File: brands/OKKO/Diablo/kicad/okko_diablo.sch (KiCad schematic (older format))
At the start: 65 parts, among them P1 1M Log, P2 1M Lin, P3 1M Log, P4 100k Log, P5 100k Lin, P6 100k Lin, Q1 J201, Q2 J201, Q3 J201, Q4 J201, Q5 J201, Q6 J201, Q7 J201, T1 100k, T2 10k Log, T3 100k Log, T4 100k Log, T5 100k Lin

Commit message: OKKO Diablo schematic
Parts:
- P3: value 1M Log -> 500k Log
- P6: value 100k Lin -> 100k Log
- T1: value 100k -> 100k Lin
- T2: value 10k Log -> 5k Log
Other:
- note added: "Bass"
- note added: "Bass+"
- note added: "Body"
- note added: "Feed"
- note added: "Gain"
- note added: "Gain+"
- note added: "Level"
- note added: "Level+"
- note added: "Presence"
- note added: "Presence+"
- note added: "Tone"
- moved on the sheet: C15, C18, P6, Q7, R20, R21
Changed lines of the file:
@@
 P 3750 3250
 F 0 "T2" V 3650 3350 59  0000 C CNN
-F 1 "10k Log" H 3750 3100 59  0000 C CNN
+F 1 "5k Log" H 3750 3100 59  0000 C CNN
 F 2 "" H 3750 3250 60  0000 C CNN
 F 3 "" H 3750 3250 60  0000 C CNN
@@
 P 3050 2250
 F 0 "T1" H 2950 2350 59  0000 C CNN
-F 1 "100k" H 3050 2150 59  0000 C CNN
+F 1 "100k Lin" H 3050 2150 59  0000 C CNN
 F 2 "" H 3050 2250 60  0000 C CNN
 F 3 "" H 3050 2250 60  0000 C CNN
@@
 P 4800 5550
 F 0 "P3" V 4900 5700 59  0000 C CNN
-F 1 "1M Log" H 4800 5400 59  0000 C CNN
+F 1 "500k Log" H 4800 5400 59  0000 C CNN
 F 2 "" H 4800 5550 60  0000 C CNN
 F 3 "" H 4800 5550 60  0000 C CNN
@@
 L CAPACITOR C15
 U 1 1 54CC49C0
-P 6650 5350
-F 0 "C15" H 6650 5480 59  0000 C CNN
-F 1 "3.3n" H 6650 5210 59  0000 C CNN
-F 2 "" H 6650 5350 60  0000 C CNN
-F 3 "" H 6650 5350 60  0000 C CNN
-	1    6650 5350
+P 6650 5200
+F 0 "C15" H 6650 5330 59  0000 C CNN
+F 1 "3.3n" H 6650 5060 59  0000 C CNN
+F 2 "" H 6650 5200 60  0000 C CNN
+F 3 "" H 6650 5200 60  0000 C CNN
+	1    6650 5200
 	0    -1   1    0
 $EndComp
@@
 	6450 4700 6650 4700
 Wire Wire Line
-	6650 4450 6650 5200
+	6650 4450 6650 5050
 $Comp
 L POTENTIOMETER P5
@@
 Connection ~ 7450 4950
 Wire Wire Line
-	6900 4950 6650 4950
+	6650 4950 6900 4950
 $Comp
 L RESISTOR R20
 U 1 1 54CC9ED9
-P 7800 5050
-F 0 "R20" H 7800 5150 59  0000 C CNN
-F 1 "1M" H 7800 4950 59  0000 C CNN
-F 2 "" H 7650 5090 60  0000 C CNN
-F 3 "" H 7650 5090 60  0000 C CNN
-	1    7800 5050
+P 7950 5200
+F 0 "R20" H 7950 5300 59  0000 C CNN
+F 1 "1M" H 7950 5100 59  0000 C CNN
+F 2 "" H 7800 5240 60  0000 C CNN
+F 3 "" H 7800 5240 60  0000 C CNN
+	1    7950 5200
 	0    -1   -1   0
 $EndComp
@@
 L NJFET Q7
 U 1 1 54CC9F62
-P 8300 4700
-F 0 "Q7" H 8140 4590 59  0000 R CNN
-F 1 "J201" H 8140 4910 59  0000 R CNN
-F 2 "TO92" H 8030 4820 29  0001 C CNN
-F 3 "" H 8175 4750 60  0000 C CNN
-	1    8300 4700
+P 8450 4700
+F 0 "Q7" H 8290 4590 59  0000 R CNN
+F 1 "J201" H 8290 4910 59  0000 R CNN
+F 2 "TO92" H 8180 4820 29  0001 C CNN
+F 3 "" H 8325 4750 60  0000 C CNN
+	1    8450 4700
 	1    0    0    -1
 $EndComp
@@
 L GND #PWR024
 U 1 1 54CC9FF4
-P 7800 5250
-F 0 "#PWR024" H 7800 5350 30  0001 C CNN
-F 1 "GND" H 7800 5100 30  0001 C CNN
-F 2 "" H 7800 5250 60  0000 C CNN
-F 3 "" H 7800 5250 60  0000 C CNN
-	1    7800 5250
+P 7950 5400
+F 0 "#PWR024" H 7950 5500 30  0001 C CNN
+F 1 "GND" H 7950 5250 30  0001 C CNN
+F 2 "" H 7950 5400 60  0000 C CNN
+F 3 "" H 7950 5400 60  0000 C CNN
+	1    7950 5400
 	1    0    0    -1
 $EndComp
@@
 L V+ #PWR025
 U 1 1 54CCA035
-P 8300 4400
-F 0 "#PWR025" H 8300 4370 20  0001 C CNN
-F 1 "V+" H 8300 4530 59  0000 C CNN
-F 2 "" H 8300 4400 60  0000 C CNN
-F 3 "" H 8300 4400 60  0000 C CNN
-	1    8300 4400
-	1    0    0    -1
-$EndComp
-Wire Wire Line
-	7600 4700 8000 4700
-Wire Wire Line
-	7800 4850 7800 4700
-Connection ~ 7800 4700
+P 8450 4400
+F 0 "#PWR025" H 8450 4370 20  0001 C CNN
+F 1 "V+" H 8450 4530 59  0000 C CNN
+F 2 "" H 8450 4400 60  0000 C CNN
+F 3 "" H 8450 4400 60  0000 C CNN
+	1    8450 4400
+	1    0    0    -1
+$EndComp
+Wire Wire Line
+	7600 4700 8150 4700
+Wire Wire Line
+	7950 4700 7950 5000
+Connection ~ 7950 4700
 $Comp
 L RESISTOR R21
 U 1 1 54CCA8A4
-P 8300 5200
-F 0 "R21" H 8300 5300 59  0000 C CNN
-F 1 "4.7k" H 8300 5100 59  0000 C CNN
-F 2 "" H 8150 5240 60  0000 C CNN
-F 3 "" H 8150 5240 60  0000 C CNN
-	1    8300 5200
+P 8450 5200
+F 0 "R21" H 8450 5300 59  0000 C CNN
+F 1 "4.7k" H 8450 5100 59  0000 C CNN
+F 2 "" H 8300 5240 60  0000 C CNN
+F 3 "" H 8300 5240 60  0000 C CNN
+	1    8450 5200
 	0    -1   1    0
 $EndComp
@@
 L GND #PWR026
 U 1 1 54CCA9B3
-P 8300 5400
-F 0 "#PWR026" H 8300 5500 30  0001 C CNN
-F 1 "GND" H 8300 5250 30  0001 C CNN
-F 2 "" H 8300 5400 60  0000 C CNN
-F 3 "" H 8300 5400 60  0000 C CNN
-	1    8300 5400
+P 8450 5400
+F 0 "#PWR026" H 8450 5500 30  0001 C CNN
+F 1 "GND" H 8450 5250 30  0001 C CNN
+F 2 "" H 8450 5400 60  0000 C CNN
+F 3 "" H 8450 5400 60  0000 C CNN
+	1    8450 5400
 	1    0    0    -1
 $EndComp
@@
 L CAPACITOR C18
 U 1 1 54CCAB4B
-P 8650 4950
-F 0 "C18" H 8650 5080 59  0000 C CNN
-F 1 "100n" H 8650 4810 59  0000 C CNN
-F 2 "" H 8650 4950 60  0000 C CNN
-F 3 "" H 8650 4950 60  0000 C CNN
-	1    8650 4950
+P 8800 4950
+F 0 "C18" H 8800 5080 59  0000 C CNN
+F 1 "100n" H 8800 4810 59  0000 C CNN
+F 2 "" H 8800 4950 60  0000 C CNN
+F 3 "" H 8800 4950 60  0000 C CNN
+	1    8800 4950
 	-1   0    0    -1
 $EndComp
 Wire Wire Line
-	8300 4900 8300 5000
-Wire Wire Line
-	8300 4950 8500 4950
-Connection ~ 8300 4950
+	8450 4900 8450 5000
+Wire Wire Line
+	8450 4950 8650 4950
+Connection ~ 8450 4950
 $Comp
 L POTENTIOMETER P6
 U 1 1 54CCB094
-P 9050 5200
-F 0 "P6" V 9150 5350 59  0000 C CNN
-F 1 "100k Lin" H 9050 5050 59  0000 C CNN
-F 2 "" H 9050 5200 60  0000 C CNN
-F 3 "" H 9050 5200 60  0000 C CNN
-	1    9050 5200
+P 9200 5200
+F 0 "P6" V 9300 5350 59  0000 C CNN
+F 1 "100k Log" H 9200 5050 59  0000 C CNN
+F 2 "" H 9200 5200 60  0000 C CNN
+F 3 "" H 9200 5200 60  0000 C CNN
+	1    9200 5200
 	0    1    1    0
 $EndComp
 Wire Wire Line
-	9050 5000 9050 4950
-Wire Wire Line
-	9050 4950 8800 4950
+	9200 5000 9200 4950
+Wire Wire Line
+	9200 4950 8950 4950
 $Comp
 L GND #PWR027
 U 1 1 54CCB670
-P 9050 5400
-F 0 "#PWR027" H 9050 5500 30  0001 C CNN
-F 1 "GND" H 9050 5250 30  0001 C CNN
-F 2 "" H 9050 5400 60  0000 C CNN
-F 3 "" H 9050 5400 60  0000 C CNN
-	1    9050 5400
+P 9200 5400
+F 0 "#PWR027" H 9200 5500 30  0001 C CNN
+F 1 "GND" H 9200 5250 30  0001 C CNN
+F 2 "" H 9200 5400 60  0000 C CNN
+F 3 "" H 9200 5400 60  0000 C CNN
+	1    9200 5400
 	1    0    0    -1
 $EndComp
@@
 	4600 2700 4500 2700
 Wire Wire Line
-	6650 5500 6850 5500
-Wire Wire Line
-	6850 5500 6850 5800
+	6850 5450 6850 5800
 Wire Wire Line
 	6850 5800 6750 5800
-Text Label 2250 2850 2    60   ~ 0
+Text Label 2250 2850 2    60   ~ 12
 BoostIn
-Text Label 5250 2300 0    60   ~ 0
+Text Label 5250 2300 0    60   ~ 12
 BoostOut
 Wire Wire Line
 	5250 2300 5050 2300
-Text Label 1550 5250 2    60   ~ 0
+Text Label 1550 5250 2    60   ~ 12
 MainIn
 Connection ~ 1750 5250
-Text Label 9400 5200 0    60   ~ 0
+Text Label 9550 5200 0    60   ~ 12
 MainOut
 Wire Wire Line
-	9400 5200 9200 5200
+	9550 5200 9350 5200
+Wire Wire Line
+	6650 5500 6650 5350
+Wire Wire Line
+	6650 5450 6850 5450
+Connection ~ 6650 5450
+Connection ~ 7450 5900
+Connection ~ 3750 3050
+Connection ~ 4400 2400
+Text Notes 1250 5600 0    79   ~ 16
+Feed
+Text Notes 4400 4850 0    79   ~ 16
+Body
+Text Notes 4300 5600 0    79   ~ 16
+Gain
+Text Notes 7600 4550 0    79   ~ 16
+Tone
+Text Notes 8650 5350 0    79   ~ 16
+Level
+Text Notes 4900 1900 0    79   ~ 16
+Level+
+Text Notes 2500 2350 0    59   ~ 12
+Bass+
+Text Notes 4000 3250 0    59   ~ 12
+Gain+
+Text Notes 4550 2850 0    59   ~ 12
+Presence+
+Text Notes 6450 6150 0    59   ~ 12
+Presence
+Text Notes 7350 6150 0    59   ~ 12
+Bass
 $EndSCHEMATC

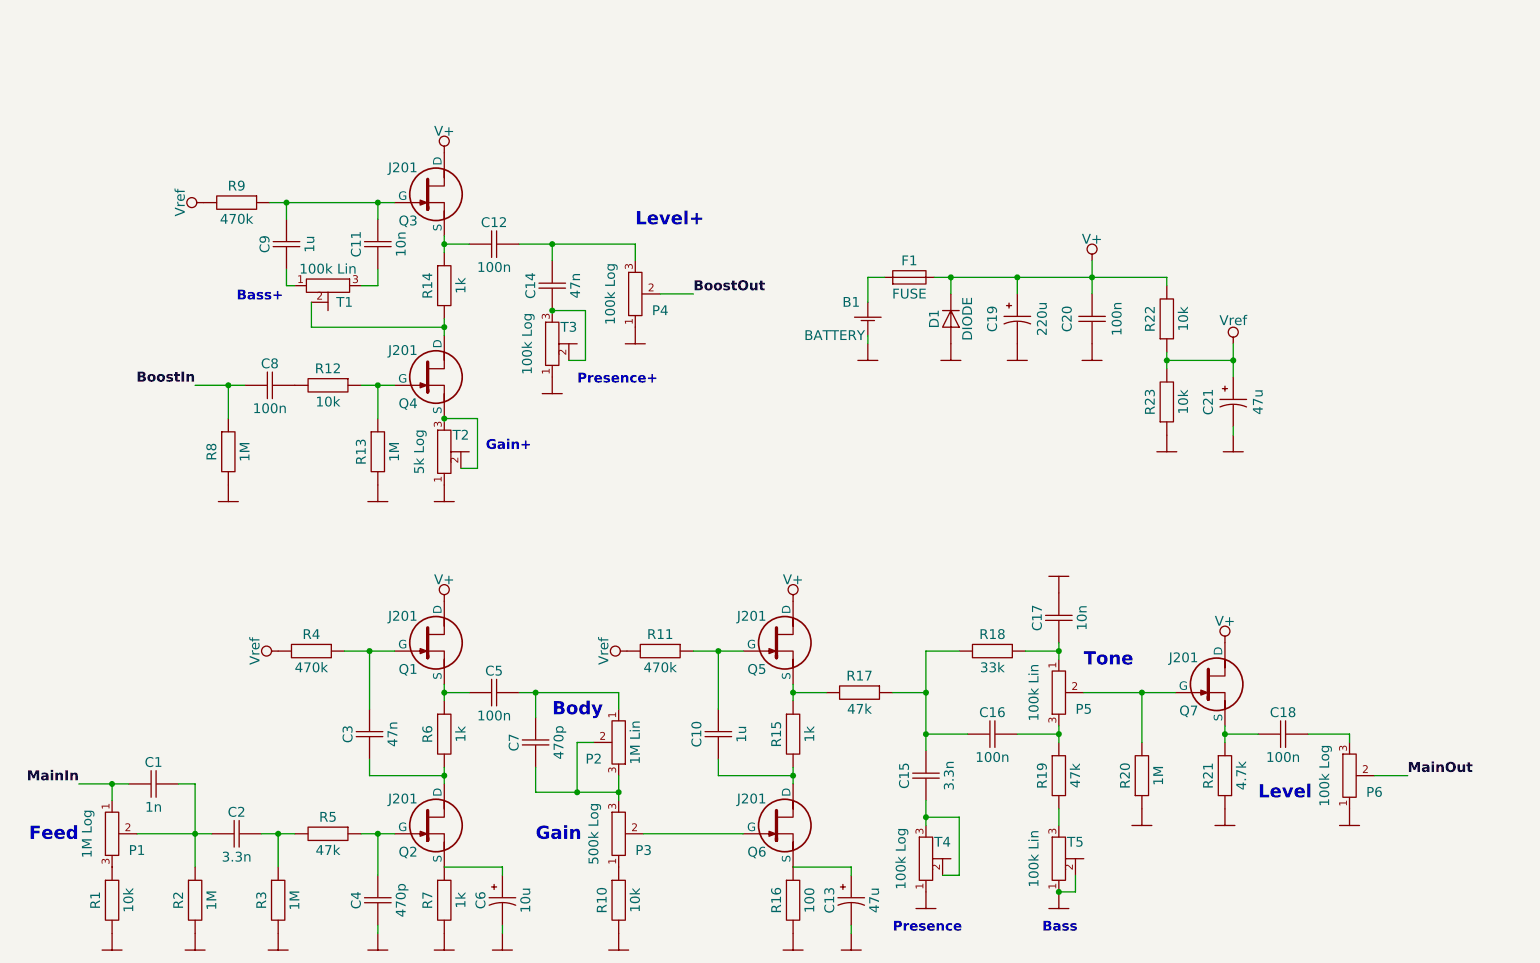
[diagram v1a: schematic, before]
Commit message: OKKO Diablo schematic correction
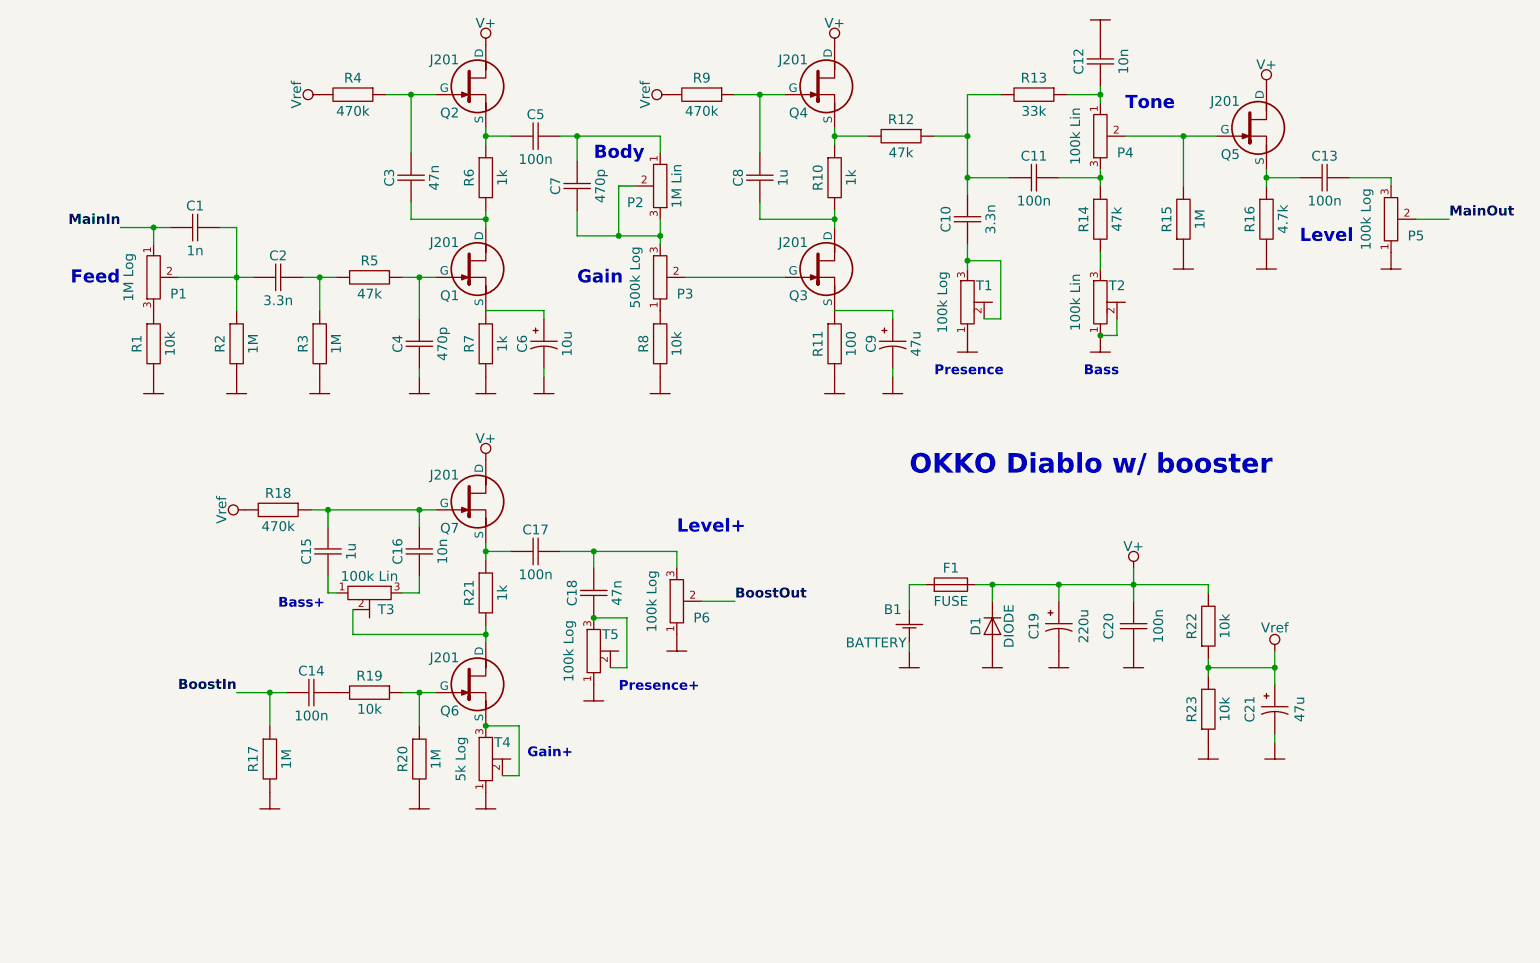
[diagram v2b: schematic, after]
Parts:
- renumbered C15 to C10, C16 to C11, C17 to C12, C18 to C13, C8 to C14, C9 to C15, C11 to C16, C12 to C17, C14 to C18, C10 to C8, C13 to C9, P5 to P4, P6 to P5, P4 to P6, Q2 to Q1, Q1 to Q2, Q6 to Q3, Q5 to Q4, Q7 to Q5, Q4 to Q6, Q3 to Q7, R15 to R10, R16 to R11, R17 to R12, R18 to R13, R19 to R14, R20 to R15, R21 to R16, R8 to R17, R9 to R18, R12 to R19, R13 to R20, R14 to R21, R10 to R8, R11 to R9, T4 to T1, T5 to T2, T1 to T3, T2 to T4, T3 to T5
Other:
- note added: "OKKO Diablo w/ booster"
- moved on the sheet: B1, C1, C10, C11, C12, C13, C14, C15, C16, C17, C18, C19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
